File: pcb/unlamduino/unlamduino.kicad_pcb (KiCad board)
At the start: 2 copper layers, 100.3 x 69.8 mm, 41 parts, among them IC2 ATMEGA328-P, P3 CONN_01X08, U1 LM2576, U2 AP111733, Y2 16MHz

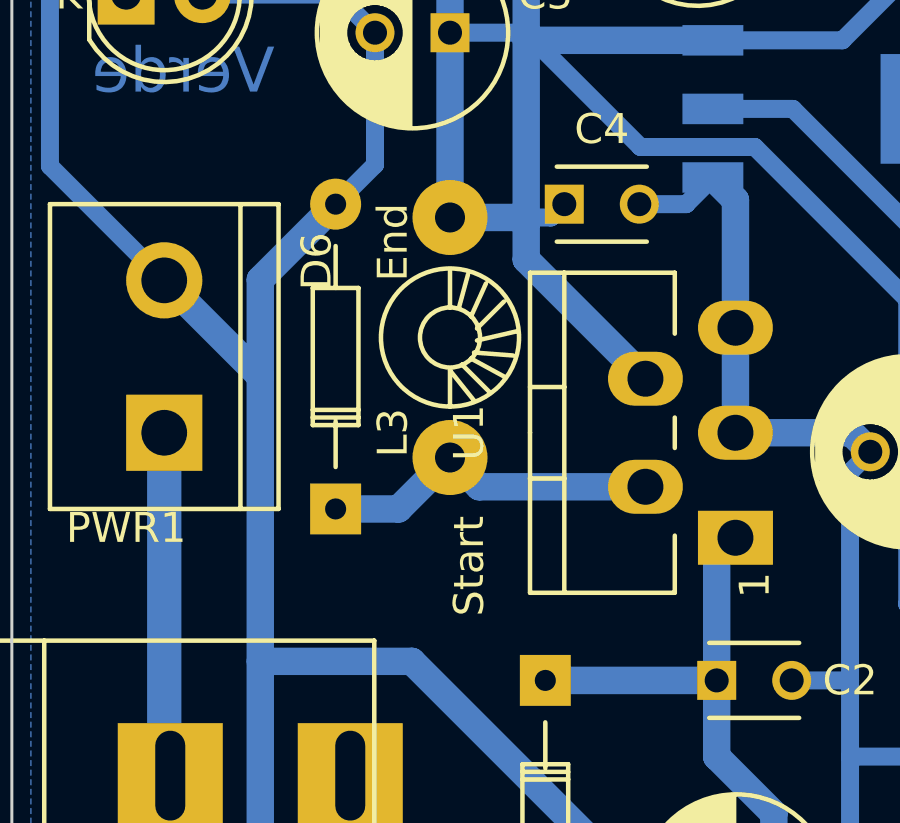
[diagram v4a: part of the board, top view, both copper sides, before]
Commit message: Corrección separación de patas del inductor de la fuente.
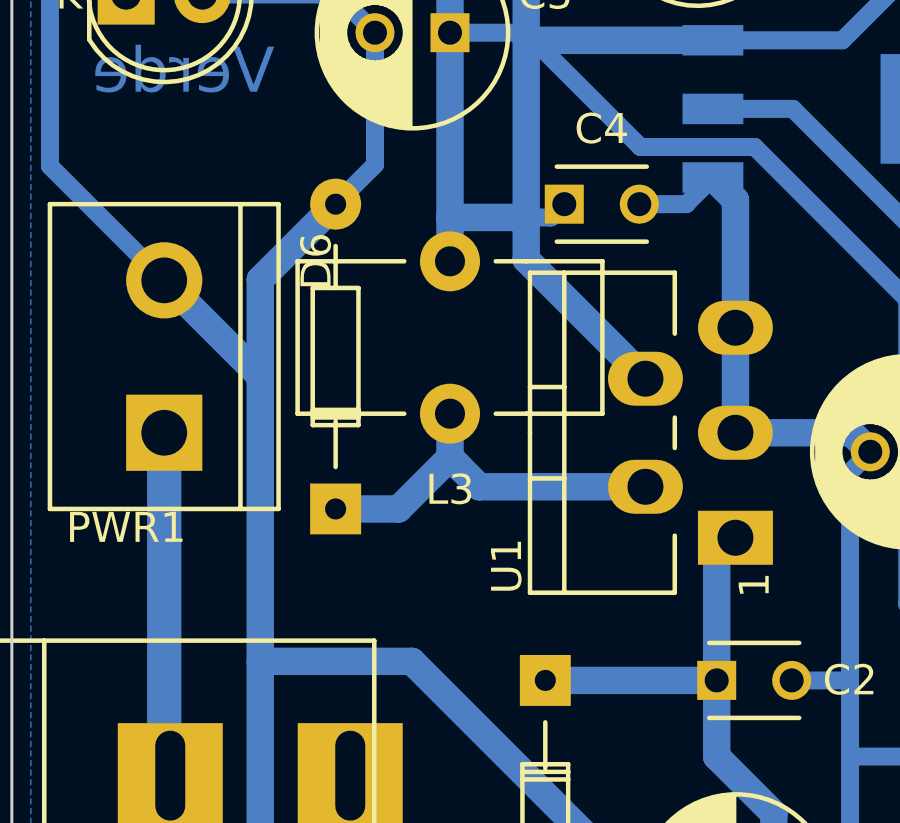
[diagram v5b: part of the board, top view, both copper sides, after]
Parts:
- L3: footprint Choke_Toroid_ThroughHole:Choke_Toroid_horizontal_Diameter4-5mm_Amidon-T16 -> Choke_Toroid_ThroughHole:Choke_Toroid_5x10mm_Vertical
- moved L3 5.68 mm to (167.6, 83.8), turned to 0 degrees
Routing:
- net +5V: track 313.4 -> 314.9 mm
- net Net-(D6-Pad1): track 16.3 -> 17.2 mm
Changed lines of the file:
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@@
     (descr "Pentawatt, Neutral, Staggered, Verical, TO220-5, T05D,")
     (tags "Pentawatt, Neutral, Staggered, Verical, TO220-5, T05D,")
-    (fp_text reference U1 (at 0 -5.08 90) (layer F.SilkS)
+    (fp_text reference U1 (at -4.445 -3.81 90) (layer F.SilkS)
       (effects (font (size 1 1) (thickness 0.15)))
     )
@@
       (rotate (xyz 0 0 0))
     )
-  )
-  (module Choke_Toroid_ThroughHole:Choke_Toroid_horizontal_Diameter4-5mm_Amidon-T16 (layer F.Cu)
-    (at 172.72 81.28 90)
-    (descr "Choke, Inductance, Toroid, horizontal, laying, Diameter 4,5mm, Amidon, T16,")
-    (tags "Choke, Inductance, Toroid, horizontal, laying, Diameter 4,5mm, Amidon, T160,")
-    (fp_text reference L3 (at -3.175 -1.905 90) (layer F.SilkS)
-      (effects (font (size 1 1) (thickness 0.15)))
-    )
-    (fp_text value 330uHy (at -8.255 -0.635 90) (layer F.Fab)
-      (effects (font (size 1 1) (thickness 0.15)))
-    )
-    (fp_line (start 1.00076 0) (end 2.19964 0) (layer F.SilkS) (width 0.15))
-    (fp_line (start 1.00076 0.29972) (end 2.10058 0.59944) (layer F.SilkS) (width 0.15))
-    (fp_line (start 0.70104 0.70104) (end 1.80086 1.19888) (layer F.SilkS) (width 0.15))
-    (fp_line (start 0.29972 0.89916) (end 1.19888 1.80086) (layer F.SilkS) (width 0.15))
-    (fp_line (start -0.09906 0.89916) (end 0.20066 2.19964) (layer F.SilkS) (width 0.15))
-    (fp_line (start -0.50038 0.8001) (end -0.59944 2.10058) (layer F.SilkS) (width 0.15))
-    (fp_line (start -0.70104 0.70104) (end -1.30048 1.80086) (layer F.SilkS) (width 0.15))
-    (fp_line (start -0.89916 0.39878) (end -1.80086 1.30048) (layer F.SilkS) (width 0.15))
-    (fp_line (start -2.30124 0) (end -1.09982 0) (layer F.SilkS) (width 0.15))
-    (fp_line (start -1.09982 0) (end -2.10058 0.8001) (layer F.SilkS) (width 0.15))
-    (fp_circle (center 0 0) (end 1.00076 0) (layer F.SilkS) (width 0.15))
-    (fp_circle (center 0 0) (end 2.30124 0) (layer F.SilkS) (width 0.15))
-    (fp_text user End (at 3.175 -1.905 90) (layer F.SilkS)
-      (effects (font (size 1 1) (thickness 0.15)))
-    )
-    (fp_text user Start (at -7.62 0.635 90) (layer F.SilkS)
-      (effects (font (size 1 1) (thickness 0.15)))
-    )
-    (pad 1 thru_hole circle (at -4.0005 0 90) (size 2.49936 2.49936) (drill 1.00076) (layers *.Cu *.Mask F.SilkS)
-      (net 18 "Net-(D6-Pad1)"))
-    (pad 2 thru_hole circle (at 4.0005 0 90) (size 2.49936 2.49936) (drill 1.00076) (layers *.Cu *.Mask F.SilkS)
-      (net 9 +5V))
   )
   (module Capacitors_ThroughHole:C_Disc_D3_P2.5 (layer F.Cu)
@@
     (fp_circle (center 0 0) (end 3.45 0) (layer F.CrtYd) (width 0.05))
     (pad 1 np_thru_hole circle (at 0 0) (size 3.2 3.2) (drill 3.2) (layers *.Cu *.Mask F.SilkS))
+  )
+  (module Choke_Toroid_ThroughHole:Choke_Toroid_5x10mm_Vertical (layer F.Cu)
+    (at 167.64 83.82)
+    (descr "Toroid, Coil, Choke,  5mm x 10mm, Vertical, Inductor, Drossel, Thruhole,")
+    (tags "Toroid, Coil, Choke, 5mm x 10mm, Vertical, Inductor, Drossel, Thruhole,")
+    (fp_text reference L3 (at 5.08 2.54) (layer F.SilkS)
+      (effects (font (size 1 1) (thickness 0.15)))
+    )
+    (fp_text value 330uHy (at 5.08 1.27) (layer F.Fab)
+      (effects (font (size 1 1) (thickness 0.15)))
+    )
+    (fp_line (start 0 0) (end 3.556 0) (layer F.SilkS) (width 0.15))
+    (fp_line (start 0 -5.08) (end 3.556 -5.08) (layer F.SilkS) (width 0.15))
+    (fp_line (start 7.62 0) (end 6.604 0) (layer F.SilkS) (width 0.15))
+    (fp_line (start 7.62 -5.08) (end 6.604 -5.08) (layer F.SilkS) (width 0.15))
+    (fp_line (start 10.16 0) (end 7.62 0) (layer F.SilkS) (width 0.15))
+    (fp_line (start 10.16 -5.08) (end 7.62 -5.08) (layer F.SilkS) (width 0.15))
+    (fp_line (start 10.16 0) (end 10.16 -5.08) (layer F.SilkS) (width 0.15))
+    (fp_line (start 0 -5.08) (end 0 0) (layer F.SilkS) (width 0.15))
+    (pad 1 thru_hole circle (at 5.08 0) (size 1.99898 1.99898) (drill 1.00076) (layers *.Cu *.Mask F.SilkS)
+      (net 18 "Net-(D6-Pad1)"))
+    (pad 2 thru_hole circle (at 5.08 -5.08) (size 1.99898 1.99898) (drill 1.00076) (layers *.Cu *.Mask F.SilkS)
+      (net 9 +5V))
   )
   (gr_text 3 (at 233.045 49.53) (layer B.Cu)
@@
   (segment (start 181.61 88.57996) (end 182.23484 87.95512) (width 0.6) (layer B.Cu) (net 8) (status 30))
   (segment (start 175.89754 92.71052) (end 181.28944 92.71052) (width 0.9144) (layer B.Cu) (net 8) (status 30))
+  (segment (start 172.72 78.74) (end 172.72 77.2795) (width 0.9144) (layer B.Cu) (net 9))
   (segment (start 207.645 100.965) (end 207.645 97.79) (width 0.6) (layer B.Cu) (net 9) (status 10))
   (segment (start 210.82 97.79) (end 207.645 97.79) (width 0.6) (layer B.Cu) (net 9) (status 10))
@@
   (segment (start 181.483 71.374) (end 181.991 71.374) (width 0.6) (layer B.Cu) (net 9) (status 30))
   (segment (start 172.72 71.12) (end 172.72 77.9145) (width 0.6) (layer B.Cu) (net 9) (status 30))
-  (segment (start 172.72 77.9145) (end 172.72 77.2795) (width 0.6) (layer B.Cu) (net 9) (status 30))
   (segment (start 172.72 71.12) (end 172.72 67.945) (width 0.6) (layer B.Cu) (net 9) (status 10))
   (segment (start 172.72 67.945) (end 175.26 65.405) (width 0.6) (layer B.Cu) (net 9) (status 20))
@@
   (segment (start 218.44 76.2) (end 220.98 73.66) (width 0.6) (layer B.Cu) (net 9))
   (segment (start 215.265 100.965) (end 215.265 101.6) (width 0.9144) (layer B.Cu) (net 9) (status 30))
+  (segment (start 172.72 77.9145) (end 172.72 77.2795) (width 0.6) (layer B.Cu) (net 9) (status 30))
   (segment (start 234.95 44.45) (end 233.68 44.45) (width 0.6) (layer B.Cu) (net 10))
   (segment (start 182.88 43.815) (end 177.8 48.895) (width 0.6) (layer B.Cu) (net 10))
@@
   (segment (start 163.195 84.455) (end 163.195 95.68434) (width 1.143) (layer B.Cu) (net 17) (status 30))
   (segment (start 163.195 95.68434) (end 163.39566 95.885) (width 1.143) (layer B.Cu) (net 17) (status 30))
+  (segment (start 172.72 85.2805) (end 172.72 83.82) (width 0.9144) (layer B.Cu) (net 18))
   (segment (start 179.2351 86.25586) (end 173.69536 86.25586) (width 0.9144) (layer B.Cu) (net 18) (status 10))
   (segment (start 173.69536 86.25586) (end 172.72 85.2805) (width 0.9144) (layer B.Cu) (net 18) (status 20))
@@
   (segment (start 171.00602 86.99448) (end 172.72 85.2805) (width 0.6) (layer B.Cu) (net 18) (status 20))
   (segment (start 173.06036 85.62086) (end 172.72 85.2805) (width 0.9144) (layer B.Cu) (net 18) (status 30))
-  (segment (start 172.52898 85.08948) (end 172.72 85.2805) (width 0.9144) (layer B.Cu) (net 18) (status 30))
-  (segment (start 172.52898 85.08948) (end 172.72 85.2805) (width 0.6) (layer B.Cu) (net 18) (status 30))
   (segment (start 179.705 67.31) (end 179.705 67.945) (width 0.6) (layer B.Cu) (net 19) (status 30))
   (segment (start 179.705 67.945) (end 180.975 69.215) (width 0.6) (layer B.Cu) (net 19) (status 10))

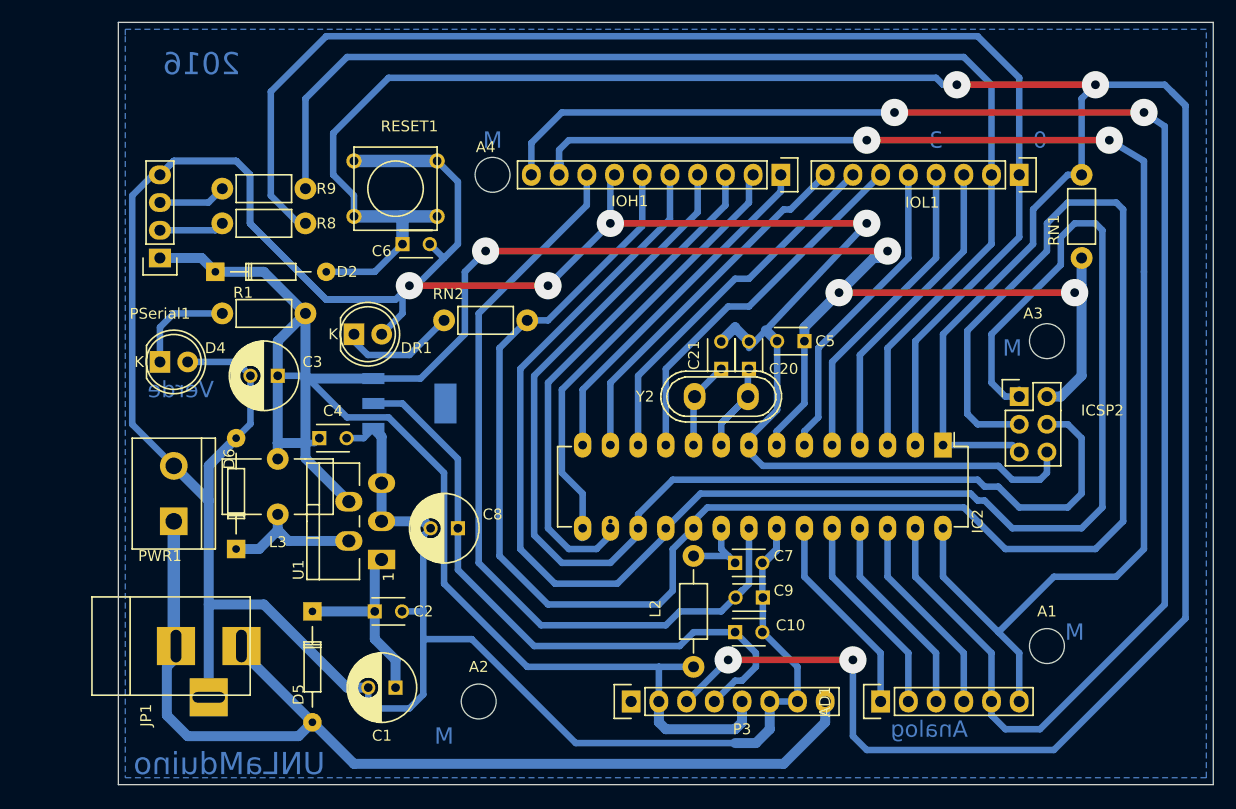
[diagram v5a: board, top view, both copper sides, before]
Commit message: Separación de pistas, añadido de puente para mejorar planchado.
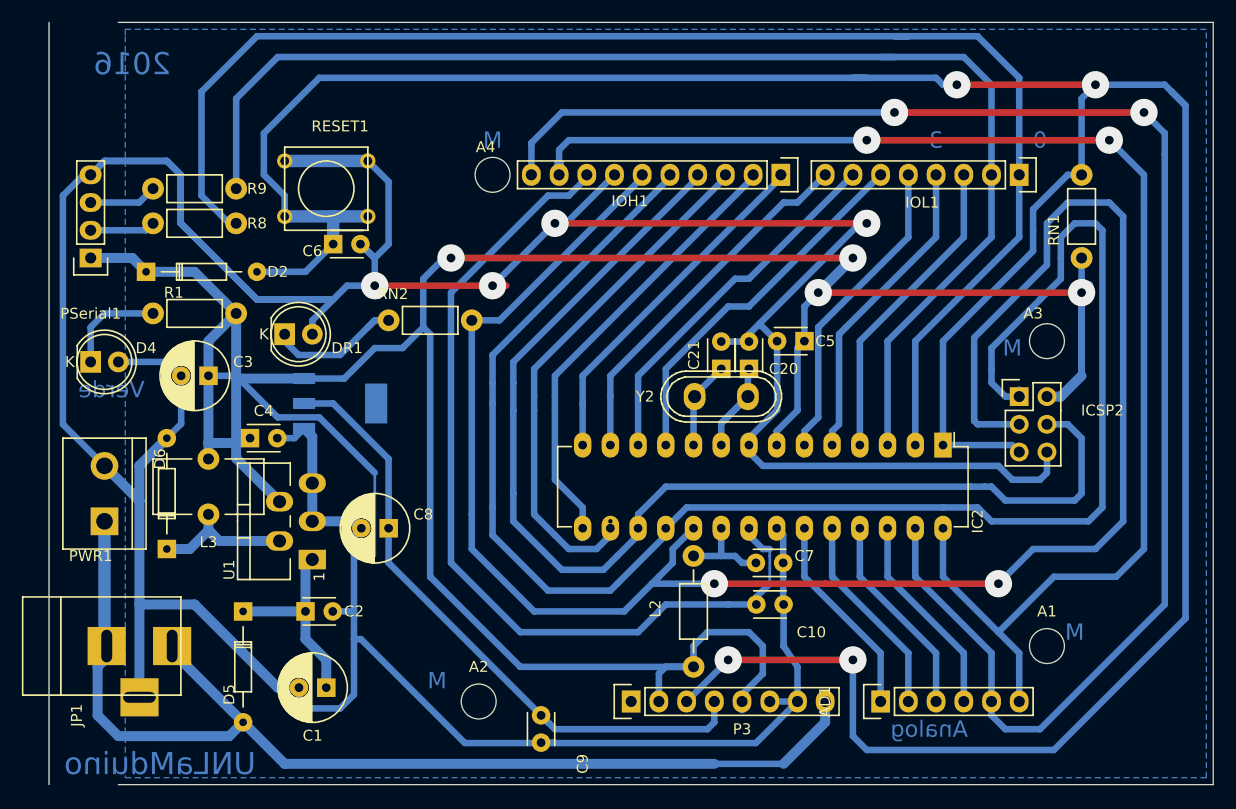
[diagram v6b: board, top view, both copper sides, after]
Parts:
- moved C9 19.3 mm to (196.8, 102.2), turned to 270 degrees
- moved C2 6.35 mm to (175.3, 92.7)
- moved D4 6.35 mm to (155.6, 69.8)
- moved D5 6.35 mm to (169.5, 92.7)
- moved DR1 6.35 mm to (173.4, 67.3)
- moved PSerial1 6.35 mm to (155.6, 60.3)
- moved C1 6.35 mm to (177.2, 99.7)
- moved C3 6.35 mm to (166.4, 71.1)
- moved C4 6.35 mm to (170.2, 76.8)
- moved C6 6.35 mm to (177.8, 59.1)
- moved C8 6.35 mm to (182.9, 85.1)
- moved D2 6.35 mm to (160.7, 61.6)
- moved D6 6.35 mm to (162.6, 87.0)
- moved JP1 6.35 mm to (156.8, 95.9)
- moved L3 6.35 mm to (161.3, 83.8)
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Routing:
- net +5V: track 314.9 -> 341.6 mm
- net GND: track 430.0 -> 449.4 mm
- net /IO1: track 110.7 -> 118.3 mm
- net /RESET: track 263.9 -> 271.5 mm
- net /VIN: track 101.9 -> 109.5 mm
- net /IO0: track 123.6 -> 131.2 mm
- net /AREF: track 75.3 -> 82.1 mm
- net /IO13: track 172.3 -> 176.4 mm, vias 0 -> 2
- net /IO12: track 150.2 -> 152.0 mm
- net /IO11: track 105.1 -> 106.5 mm
- net +3V3: track 57.9 -> 59.2 mm
- net Net-(DR1-Pad1): track 11.6 -> 12.9 mm
- net /IO9: track 41.2 -> 42.2 mm
- net /IO10: track 46.8 -> 47.8 mm
- net Net-(C7-Pad1): track 8.41 -> 9.15 mm
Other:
- board size 100.3 x 69.8 mm -> 106.7 x 69.8 mm
